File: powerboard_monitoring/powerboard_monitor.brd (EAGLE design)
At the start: 29.2 x 32.7 mm, 14 parts, among them Q1 BSS123, U1 INA3221.

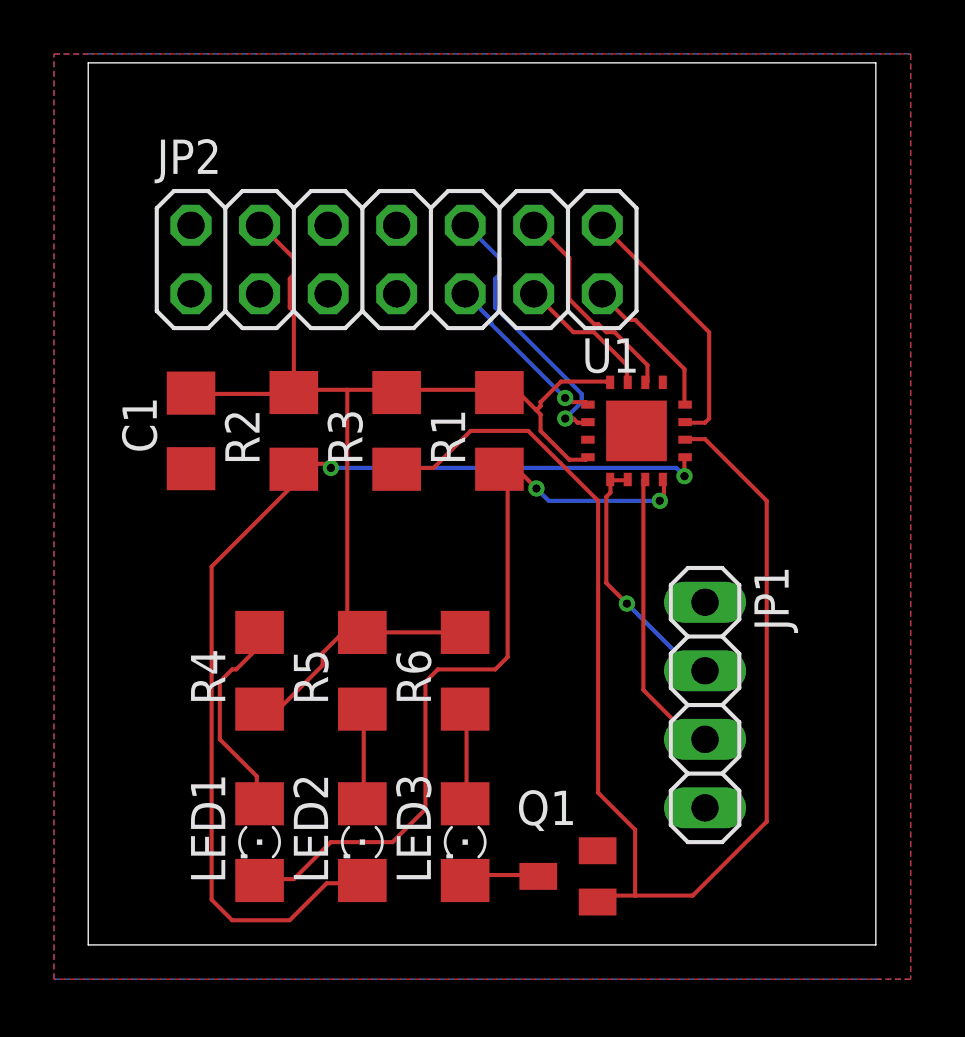
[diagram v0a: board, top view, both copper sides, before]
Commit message: Board (v.2)
The board is remade to have save space.
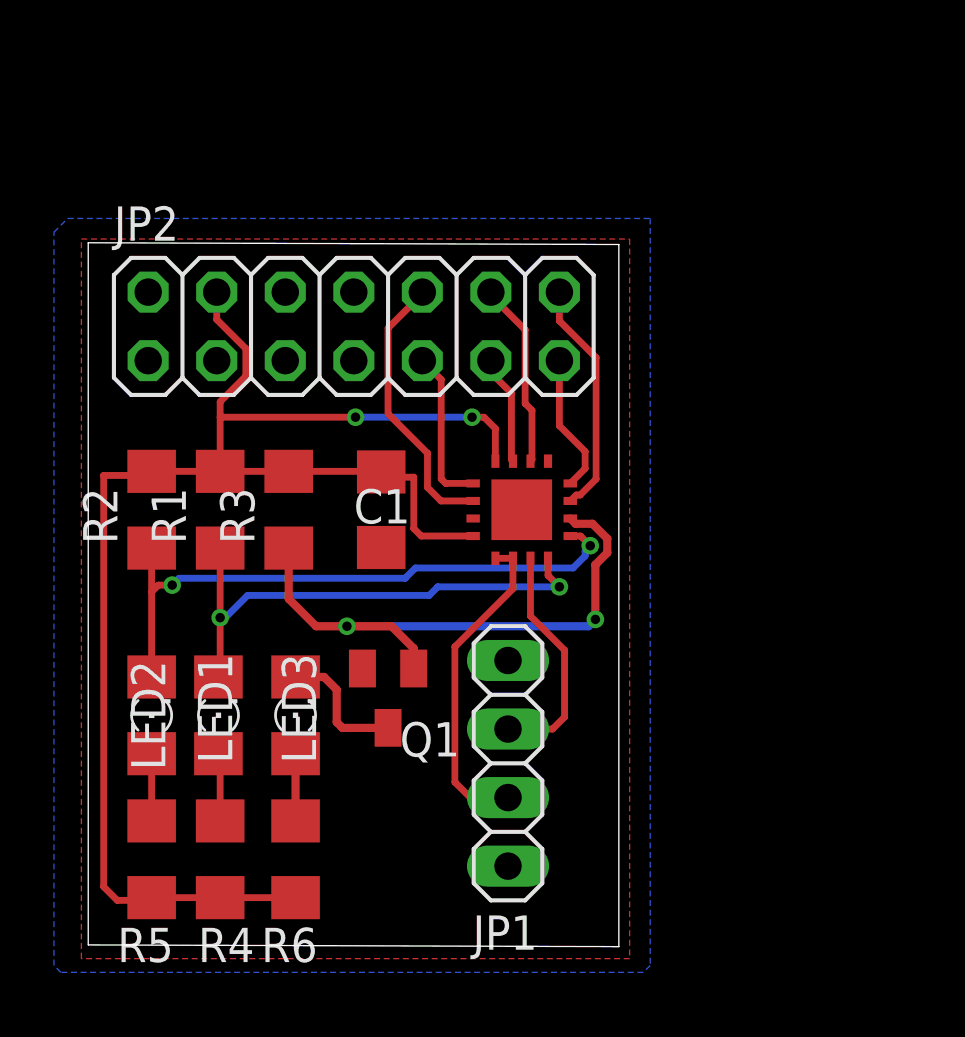
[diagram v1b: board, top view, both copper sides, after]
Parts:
- R6: value 360 Ohm -> 300 Ohm
- moved R1 10.8 mm to (4.89, 16.1)
- moved R5 10.5 mm to (2.35, 3.17), turned to 90 degrees
- moved R6 9.40 mm to (7.68, 3.17), turned to 270 degrees
- moved Q1 9.38 mm to (11.1, 9.14), turned to 180 degrees
- moved LED2 9.12 mm to (2.35, 8.51), turned to 90 degrees
- moved LED3 7.85 mm to (7.68, 8.51), turned to 90 degrees
- moved C1 7.63 mm to (10.9, 16.1)
- moved JP1 7.61 mm to (15.6, 6.73), turned to 90 degrees
- moved R4 7.14 mm to (4.89, 3.17)
- moved R2 6.03 mm to (2.35, 16.1)
- moved U1 5.16 mm to (16.1, 16.1)
- moved R3 4.95 mm to (7.43, 16.1)
- moved LED1 4.94 mm to (4.83, 8.51), turned to 90 degrees
- moved JP2 2.94 mm to (9.84, 22.9)
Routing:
- net PV_OUT: track 47.8 -> 22.2 mm, vias 0 -> 2
- net CRITICAL_OUT: track 39.2 -> 22.7 mm
- net 5V: track 45.4 -> 57.5 mm, vias 0 -> 2
- net WARNING_OUT: track 29.9 -> 19.1 mm
- net N$4: track 7.65 -> 2.52 mm
- net SCL: track 9.59 -> 12.0 mm, vias 1 -> 0
- net SDA: track 10.9 -> 8.69 mm
- net N$2: track 2.81 -> 4.92 mm
- net 5V+: track 5.19 -> 4.06 mm
- net N$5: track 3.54 -> 2.49 mm
- net N$1: track 3.54 -> 2.49 mm
- net 5V-: track 7.95 -> 6.92 mm
- net 3V-: track 9.76 -> 8.78 mm
- net 12V+: track 6.34 -> 5.92 mm, vias 1 -> 0
- net 12V-: track 10.4 -> 10.3 mm, vias 1 -> 0
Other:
- board size 29.2 x 32.7 mm -> 19.7 x 26.1 mm

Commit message: Board (v.3)
-Various traces made wider (5V, Digital outputs)
-Fixed the dimensions of the board.
Note: The board meets the design rules as uploaded by Alain on 11-24-2017
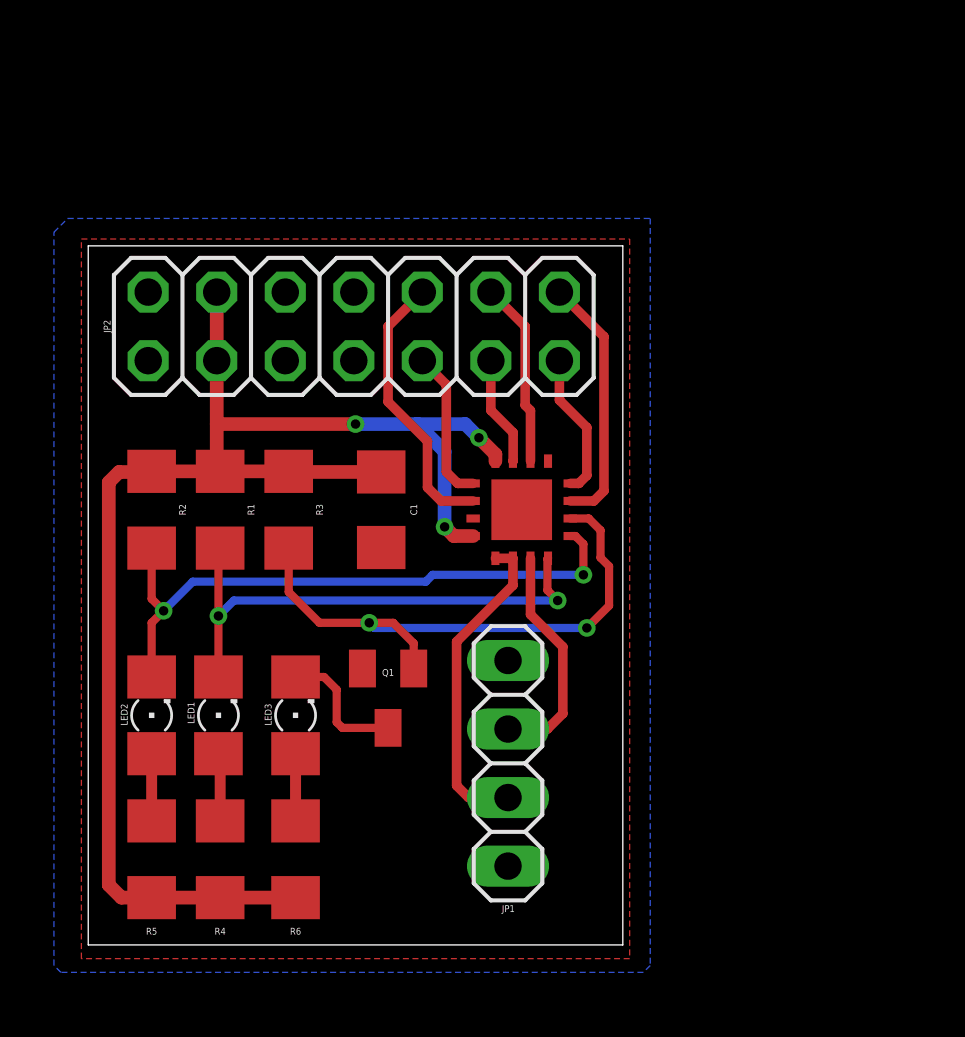
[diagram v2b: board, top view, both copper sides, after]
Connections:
- net 5V: now also JP2.3
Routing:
- net 5V: track 57.5 -> 55.4 mm, vias 2 -> 3
- net 3V-: track 8.78 -> 9.45 mm
- net PV_OUT: track 22.2 -> 21.5 mm
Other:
- board size 19.7 x 26.1 mm -> 19.8 x 25.9 mm

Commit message: Board (v.4)
Fixed the issue of islanding.
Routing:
- net GND: track 0.00 -> 8.67 mm, vias 0 -> 1
- net 5V: track 55.4 -> 56.5 mm
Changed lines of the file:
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@@
 <vertex x="-1.27" y="26.416"/>
 </polygon>
-<wire x1="10.8585" y1="14.729" x2="14.2655" y2="15.804" width="0" layer="19" extent="1-1"/>
-<wire x1="15.5575" y1="10.541" x2="14.2655" y2="15.804" width="0" layer="19" extent="1-1"/>
+<wire x1="14.2655" y1="15.804" x2="13.025" y2="15.804" width="0.1524" layer="1"/>
+<wire x1="13.025" y1="15.804" x2="12.6365" y2="16.1925" width="0.1524" layer="1"/>
+<wire x1="12.6365" y1="16.1925" x2="12.065" y2="15.621" width="0.1524" layer="1"/>
+<wire x1="12.065" y1="15.621" x2="12.065" y2="14.7955" width="0.1524" layer="1"/>
+<wire x1="12.065" y1="14.7955" x2="11.9985" y2="14.729" width="0.1524" layer="1"/>
+<wire x1="11.9985" y1="14.729" x2="10.8585" y2="14.729" width="0.1524" layer="1"/>
+<wire x1="10.1625" y1="10.244" x2="9.167" y2="11.2395" width="0.1524" layer="1"/>
+<wire x1="9.167" y1="11.2395" x2="7.112" y2="11.2395" width="0.1524" layer="1"/>
+<wire x1="7.112" y1="11.2395" x2="6.858" y2="11.4935" width="0.1524" layer="1"/>
+<wire x1="6.858" y1="11.4935" x2="6.858" y2="11.684" width="0.1524" layer="1"/>
+<via x="6.858" y="11.684" extent="1-16" drill="0.35"/>
 </signal>
 <signal name="5V">
@@
 <contactref element="R6" pad="2"/>
 <contactref element="JP2" pad="3"/>
-<wire x1="4.7625" y1="24.1935" x2="4.7625" y2="21.6535" width="0.508" layer="1"/>
-<wire x1="4.7625" y1="21.6535" x2="4.7625" y2="19.304" width="0.508" layer="1"/>
-<wire x1="4.7625" y1="17.678" x2="4.7625" y2="19.304" width="0.508" layer="1"/>
-<wire x1="4.7625" y1="17.678" x2="4.8895" y2="17.551" width="0.508" layer="1"/>
-<wire x1="4.8895" y1="17.551" x2="7.4295" y2="17.551" width="0.508" layer="1"/>
+<wire x1="4.7625" y1="21.6535" x2="4.7625" y2="24.1935" width="0.508" layer="1"/>
+<wire x1="7.4295" y1="17.551" x2="4.8895" y2="17.551" width="0.508" layer="1"/>
 <wire x1="7.4295" y1="17.551" x2="7.4515" y2="17.529" width="0.508" layer="1"/>
 <wire x1="7.4515" y1="17.529" x2="10.8585" y2="17.529" width="0.508" layer="1"/>
-<wire x1="4.7625" y1="19.304" x2="9.906" y2="19.304" width="0.508" layer="1"/>
-<via x="9.906" y="19.304" extent="1-16" drill="0.35"/>
-<wire x1="9.906" y1="19.304" x2="12.192" y2="19.304" width="0.508" layer="16"/>
-<wire x1="12.192" y1="19.304" x2="13.97" y2="19.304" width="0.508" layer="16"/>
-<wire x1="13.97" y1="19.304" x2="14.478" y2="18.796" width="0.508" layer="16"/>
-<via x="14.478" y="18.796" extent="1-16" drill="0.35"/>
-<wire x1="14.478" y1="18.796" x2="15.0905" y2="18.1835" width="0.508" layer="1"/>
-<wire x1="15.0905" y1="18.1835" x2="15.0905" y2="17.929" width="0.508" layer="1"/>
-<wire x1="12.192" y1="19.304" x2="13.208" y2="18.288" width="0.508" layer="16"/>
-<wire x1="13.208" y1="18.288" x2="13.208" y2="15.494" width="0.508" layer="16"/>
-<via x="13.208" y="15.494" extent="1-16" drill="0.35"/>
-<wire x1="13.208" y1="15.494" x2="13.548" y2="15.154" width="0.508" layer="1"/>
-<wire x1="13.548" y1="15.154" x2="14.2655" y2="15.154" width="0.508" layer="1"/>
 <wire x1="2.3245" y1="17.526" x2="2.3495" y2="17.551" width="0.508" layer="1"/>
 <wire x1="2.3245" y1="17.526" x2="1.143" y2="17.526" width="0.508" layer="1"/>
@@
 <wire x1="2.3495" y1="1.753" x2="4.8895" y2="1.753" width="0.508" layer="1"/>
 <wire x1="4.8895" y1="1.753" x2="7.6835" y2="1.753" width="0.508" layer="1"/>
-<wire x1="2.3495" y1="17.551" x2="4.6355" y2="17.551" width="0.508" layer="1"/>
-<wire x1="4.6355" y1="17.551" x2="4.7625" y2="17.678" width="0.508" layer="1"/>
+<wire x1="2.3495" y1="17.551" x2="4.8895" y2="17.551" width="0.508" layer="1"/>
+<wire x1="4.8895" y1="17.551" x2="4.7625" y2="17.678" width="0.508" layer="1"/>
+<wire x1="4.7625" y1="17.678" x2="4.7625" y2="19.304" width="0.508" layer="1"/>
+<via x="10.16" y="19.4945" extent="1-16" drill="0.35"/>
+<wire x1="4.7625" y1="19.304" x2="4.7625" y2="21.6535" width="0.508" layer="1"/>
+<wire x1="10.16" y1="19.4945" x2="12.7" y2="19.4945" width="0.508" layer="16"/>
+<via x="14.097" y="19.4945" extent="1-16" drill="0.35"/>
+<wire x1="12.7" y1="19.4945" x2="14.097" y2="19.4945" width="0.508" layer="16"/>
+<wire x1="14.097" y1="19.4945" x2="15.0905" y2="18.501" width="0.508" layer="1"/>
+<wire x1="15.0905" y1="18.501" x2="15.0905" y2="17.929" width="0.508" layer="1"/>
+<wire x1="12.7" y1="19.4945" x2="12.446" y2="19.2405" width="0.508" layer="16"/>
+<wire x1="12.446" y1="19.2405" x2="12.446" y2="15.494" width="0.508" layer="16"/>
+<wire x1="12.446" y1="15.494" x2="12.7" y2="15.24" width="0.508" layer="16"/>
+<via x="12.7" y="15.24" extent="1-16" drill="0.35"/>
+<wire x1="12.7" y1="15.24" x2="12.786" y2="15.154" width="0.508" layer="1"/>
+<wire x1="12.786" y1="15.154" x2="14.2655" y2="15.154" width="0.508" layer="1"/>
+<wire x1="4.7625" y1="19.304" x2="9.9695" y2="19.304" width="0.508" layer="1"/>
+<wire x1="9.9695" y1="19.304" x2="10.16" y2="19.4945" width="0.508" layer="1"/>
 </signal>
 <signal name="SCL">
@@
 <signal name="N$6">
 </signal>
+<signal name="N$8">
+</signal>
 </signals>

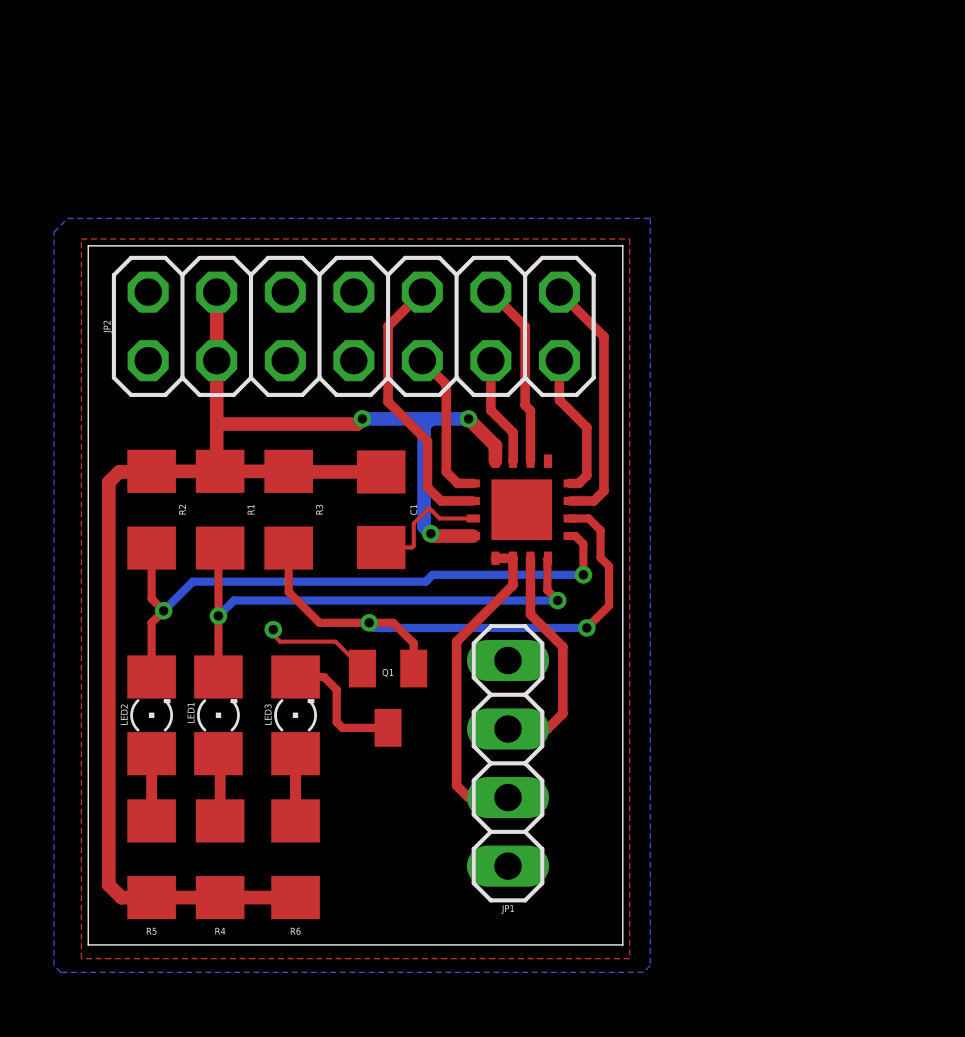
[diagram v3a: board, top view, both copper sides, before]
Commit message: Board (v.5)
Added vias from top plane to bottom plane.

Flipped the capacitor so it is closer to VS pin.
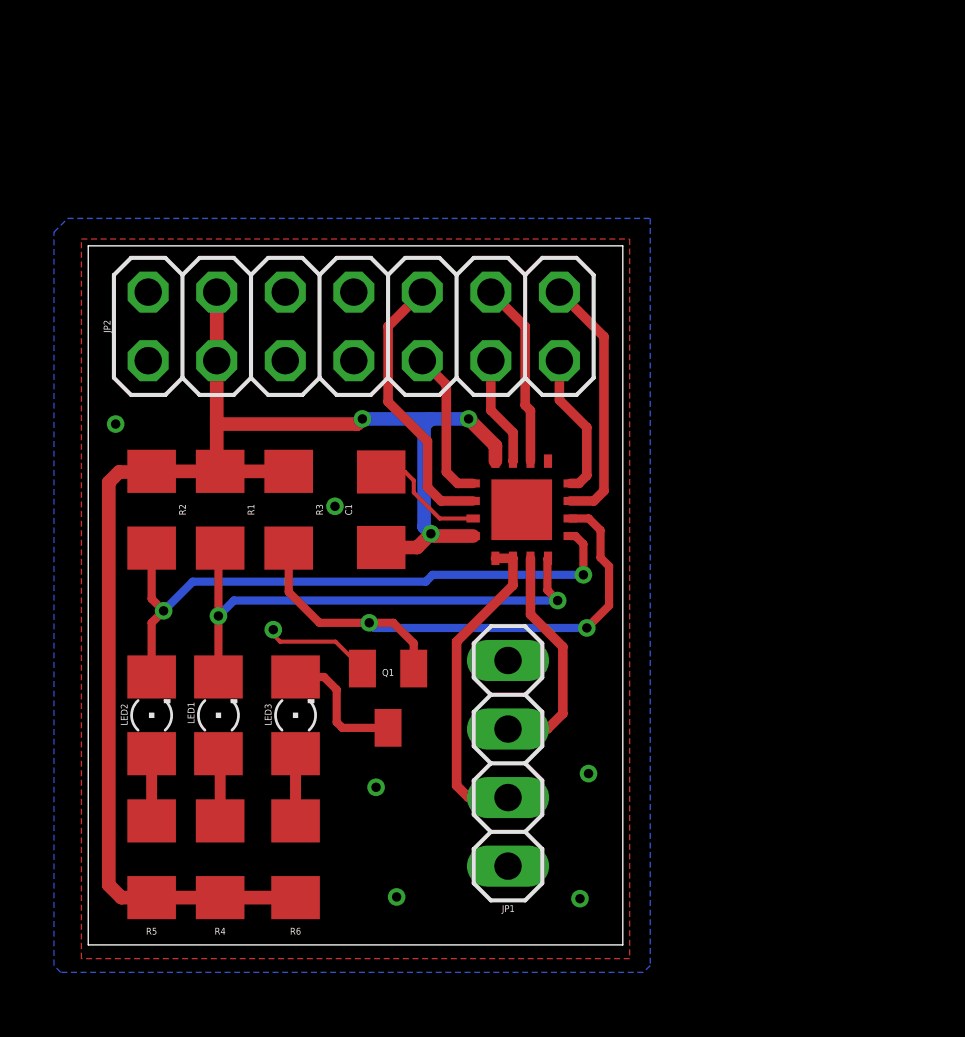
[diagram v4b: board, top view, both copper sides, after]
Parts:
- turned C1 to 90 degrees
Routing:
- net 5V: track 56.5 -> 55.1 mm
- net GND: track 8.67 -> 8.39 mm, vias 1 -> 7
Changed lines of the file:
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@@
 </autorouter>
 <elements>
-<element name="C1" library="resistor" library_urn="urn:adsk.eagle:library:348" package="C1206" package3d_urn="urn:adsk.eagle:package:26140/1" value="0.1 microF" x="10.8585" y="16.129" smashed="yes" rot="R270">
-<attribute name="NAME" x="12.065" y="16.129" size="0.254" layer="25" rot="R90" align="center"/>
+<element name="C1" library="resistor" library_urn="urn:adsk.eagle:library:348" package="C1206" package3d_urn="urn:adsk.eagle:package:26140/1" value="0.1 microF" x="10.8585" y="16.129" smashed="yes" rot="R90">
+<attribute name="NAME" x="9.652" y="16.129" size="0.254" layer="25" rot="R270" align="center"/>
 </element>
 <element name="JP1" library="pinhead" library_urn="urn:adsk.eagle:library:325" package="1X04" package3d_urn="urn:adsk.eagle:package:22407/2" value="" x="15.5575" y="6.731" smashed="yes" rot="R90">
@@
 <wire x1="14.2655" y1="15.804" x2="13.025" y2="15.804" width="0.1524" layer="1"/>
 <wire x1="13.025" y1="15.804" x2="12.6365" y2="16.1925" width="0.1524" layer="1"/>
-<wire x1="12.6365" y1="16.1925" x2="12.065" y2="15.621" width="0.1524" layer="1"/>
-<wire x1="12.065" y1="15.621" x2="12.065" y2="14.7955" width="0.1524" layer="1"/>
-<wire x1="12.065" y1="14.7955" x2="11.9985" y2="14.729" width="0.1524" layer="1"/>
-<wire x1="11.9985" y1="14.729" x2="10.8585" y2="14.729" width="0.1524" layer="1"/>
 <wire x1="10.1625" y1="10.244" x2="9.167" y2="11.2395" width="0.1524" layer="1"/>
 <wire x1="9.167" y1="11.2395" x2="7.112" y2="11.2395" width="0.1524" layer="1"/>
@@
 <wire x1="6.858" y1="11.4935" x2="6.858" y2="11.684" width="0.1524" layer="1"/>
 <via x="6.858" y="11.684" extent="1-16" drill="0.35"/>
+<wire x1="12.6365" y1="16.1925" x2="12.065" y2="16.764" width="0.1524" layer="1"/>
+<wire x1="12.065" y1="16.764" x2="12.065" y2="17.2085" width="0.1524" layer="1"/>
+<wire x1="12.065" y1="17.2085" x2="11.7445" y2="17.529" width="0.1524" layer="1"/>
+<wire x1="11.7445" y1="17.529" x2="10.8585" y2="17.529" width="0.1524" layer="1"/>
+<via x="1.016" y="19.304" extent="1-16" drill="0.35"/>
+<via x="10.668" y="5.842" extent="1-16" drill="0.35"/>
+<via x="18.542" y="6.35" extent="1-16" drill="0.35"/>
+<via x="11.43" y="1.778" extent="1-16" drill="0.35"/>
+<via x="18.2245" y="1.7145" extent="1-16" drill="0.35"/>
+<via x="9.144" y="16.256" extent="1-16" drill="0.35"/>
 </signal>
 <signal name="5V">
@@
 <wire x1="7.4295" y1="17.551" x2="4.8895" y2="17.551" width="0.508" layer="1"/>
 <wire x1="7.4295" y1="17.551" x2="7.4515" y2="17.529" width="0.508" layer="1"/>
-<wire x1="7.4515" y1="17.529" x2="10.8585" y2="17.529" width="0.508" layer="1"/>
 <wire x1="2.3245" y1="17.526" x2="2.3495" y2="17.551" width="0.508" layer="1"/>
 <wire x1="2.3245" y1="17.526" x2="1.143" y2="17.526" width="0.508" layer="1"/>
@@
 <wire x1="12.446" y1="15.494" x2="12.7" y2="15.24" width="0.508" layer="16"/>
 <via x="12.7" y="15.24" extent="1-16" drill="0.35"/>
-<wire x1="12.7" y1="15.24" x2="12.786" y2="15.154" width="0.508" layer="1"/>
+<wire x1="12.786" y1="15.154" x2="12.7" y2="15.24" width="0.508" layer="1"/>
 <wire x1="12.786" y1="15.154" x2="14.2655" y2="15.154" width="0.508" layer="1"/>
 <wire x1="4.7625" y1="19.304" x2="9.9695" y2="19.304" width="0.508" layer="1"/>
 <wire x1="9.9695" y1="19.304" x2="10.16" y2="19.4945" width="0.508" layer="1"/>
+<wire x1="12.7" y1="15.24" x2="12.189" y2="14.729" width="0.508" layer="1"/>
+<wire x1="12.189" y1="14.729" x2="10.8585" y2="14.729" width="0.508" layer="1"/>
 </signal>
 <signal name="SCL">
